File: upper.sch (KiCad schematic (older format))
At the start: 4 parts, among them SW1 SPST, U2 WIFI, U3 CAMERA, U4 RSL

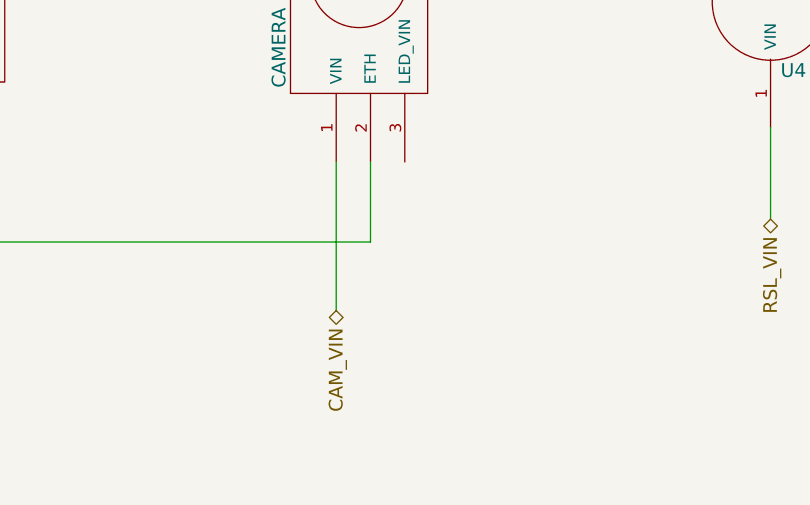
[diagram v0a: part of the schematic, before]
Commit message: Udpates to main board and start of connector spec.
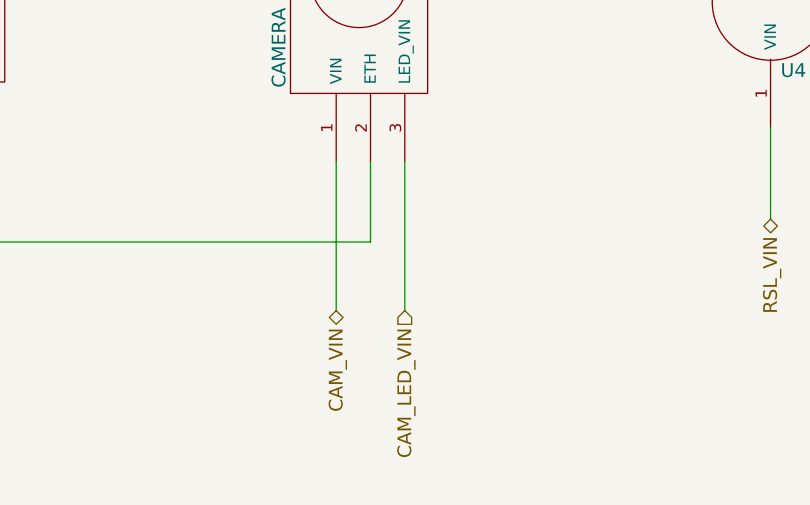
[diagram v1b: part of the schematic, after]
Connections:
- net CAM_LED_VIN: now reaches U3.3 (LED_VIN)
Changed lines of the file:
@@
 $Descr A4 11693 8268
 encoding utf-8
-Sheet 2 5
+Sheet 4 5
 Title ""
 Date "6 feb 2014"
@@
 Wire Wire Line
 	3850 3000 3850 3150
+Text HLabel 7900 3750 3    60   Input ~ 0
+CAM_LED_VIN
+Wire Wire Line
+	7900 3100 7900 3750
 $EndSCHEMATC
